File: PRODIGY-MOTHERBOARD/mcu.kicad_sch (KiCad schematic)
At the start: 24 parts, among them J1 DF40C-100DS-0.4V(51), J2 USB_C_Receptacle, J3 Conn_02x20_Odd_Even, J4 DF40C-100DS-0.4V(51), SW1 SW_Push

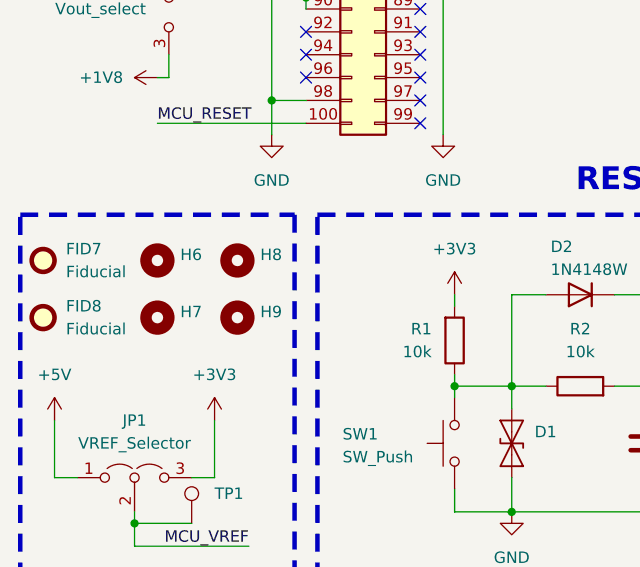
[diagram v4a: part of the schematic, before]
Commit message: ESP32 schematic complete.
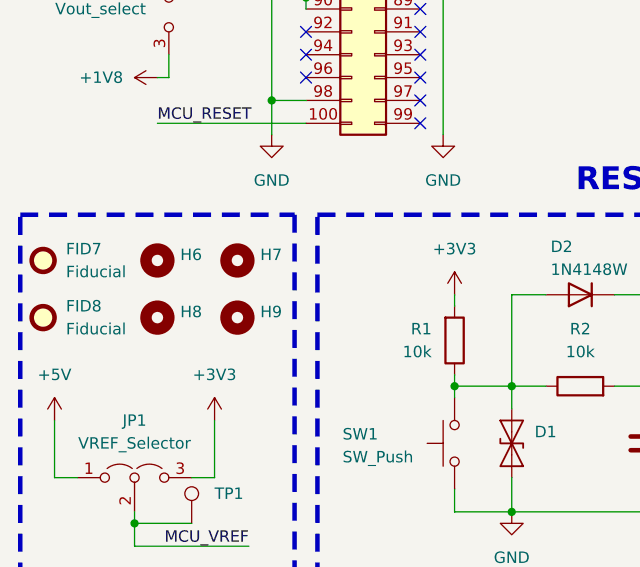
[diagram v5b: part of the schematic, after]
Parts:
- H6, H7, H8, H9: footprint MountingHole:MountingHole_3.2mm_M3_ISO7380_Pad_TopBottom -> MountingHole:MountingHole_4.3mm_M4_ISO14580_Pad

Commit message: Started STM32. Finished connectors and ST-LINK V2 schematic.
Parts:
- J1, J4: footprint (none) -> DF40C:HIROSE_DF40C-100DS-0.4V_51_
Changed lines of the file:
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@@
 			)
 		)
-		(property "Footprint" ""
+		(property "Footprint" "DF40C:HIROSE_DF40C-100DS-0.4V_51_"
 			(at 53.086 14.986 0)
 			(effects
@@
 			)
 		)
-		(property "Footprint" ""
+		(property "Footprint" "DF40C:HIROSE_DF40C-100DS-0.4V_51_"
 			(at 237.236 17.526 0)
 			(effects

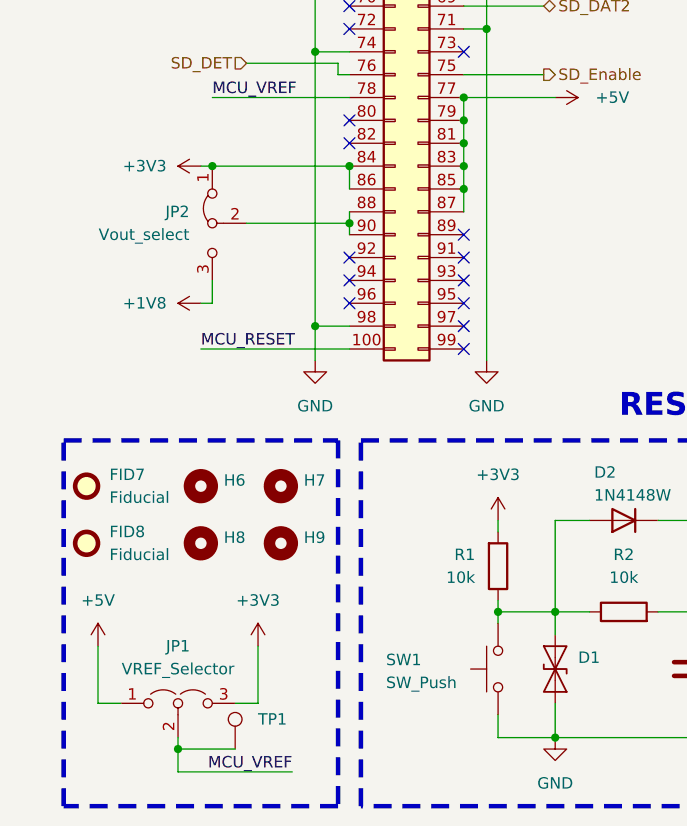
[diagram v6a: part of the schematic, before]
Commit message: Motherboard footprints assigned.
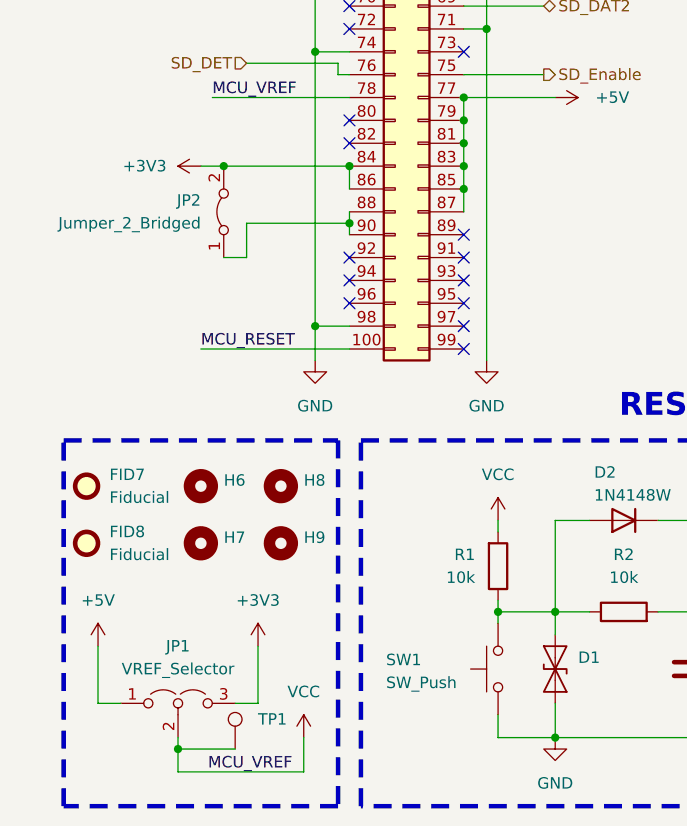
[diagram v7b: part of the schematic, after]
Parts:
- removed JP2: Vout_select, symbol Jumper:Jumper_3_Bridged12
- added JP2: Jumper_2_Bridged, Connector_PinHeader_2.54mm:PinHeader_1x02_P2.54mm_Vertical, symbol Jumper:Jumper_2_Bridged
- C1: footprint (none) -> Capacitor_SMD:C_0805_2012Metric
- FID7, FID8: footprint (none) -> Fiducial:Fiducial_1mm_Mask3mm
- JP1: footprint (none) -> Connector_PinHeader_2.54mm:PinHeader_1x03_P2.54mm_Vertical
- renumbered H8 to H7, H7 to H8
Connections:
- net +3V3: now also JP2.2 (B); no longer R1.2
- net at J1.88, J1.90: now also JP2.1 (A)
- net MCU_VREF renamed VCC
- net VCC: now also R1.2

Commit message: STM32 bom done.
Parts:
- J1, J4: TME (none) -> DF40C-100DS-0.4V51
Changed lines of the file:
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@@
 			)
 		)
-		(property "TME" ""
+		(property "TME" "DF40C-100DS-0.4V51"
 			(at 53.34 16.51 0)
 			(effects
@@
 			)
 		)
-		(property "TME" ""
+		(property "TME" "DF40C-100DS-0.4V51"
 			(at 237.49 19.05 0)
 			(effects
